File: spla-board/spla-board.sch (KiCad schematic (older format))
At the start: 0 parts

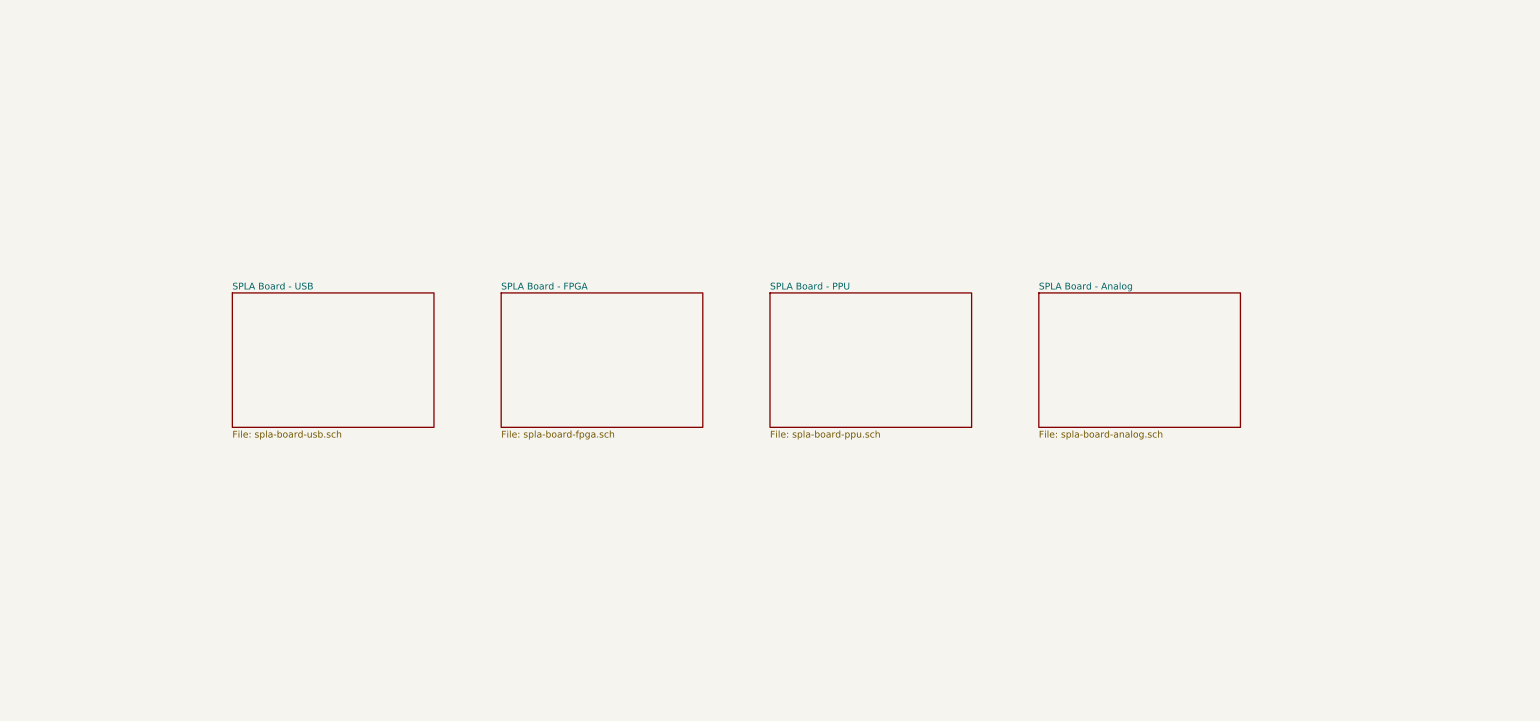
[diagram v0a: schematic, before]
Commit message: schematic: Add blank sheets for future components; rearrange root sheet.
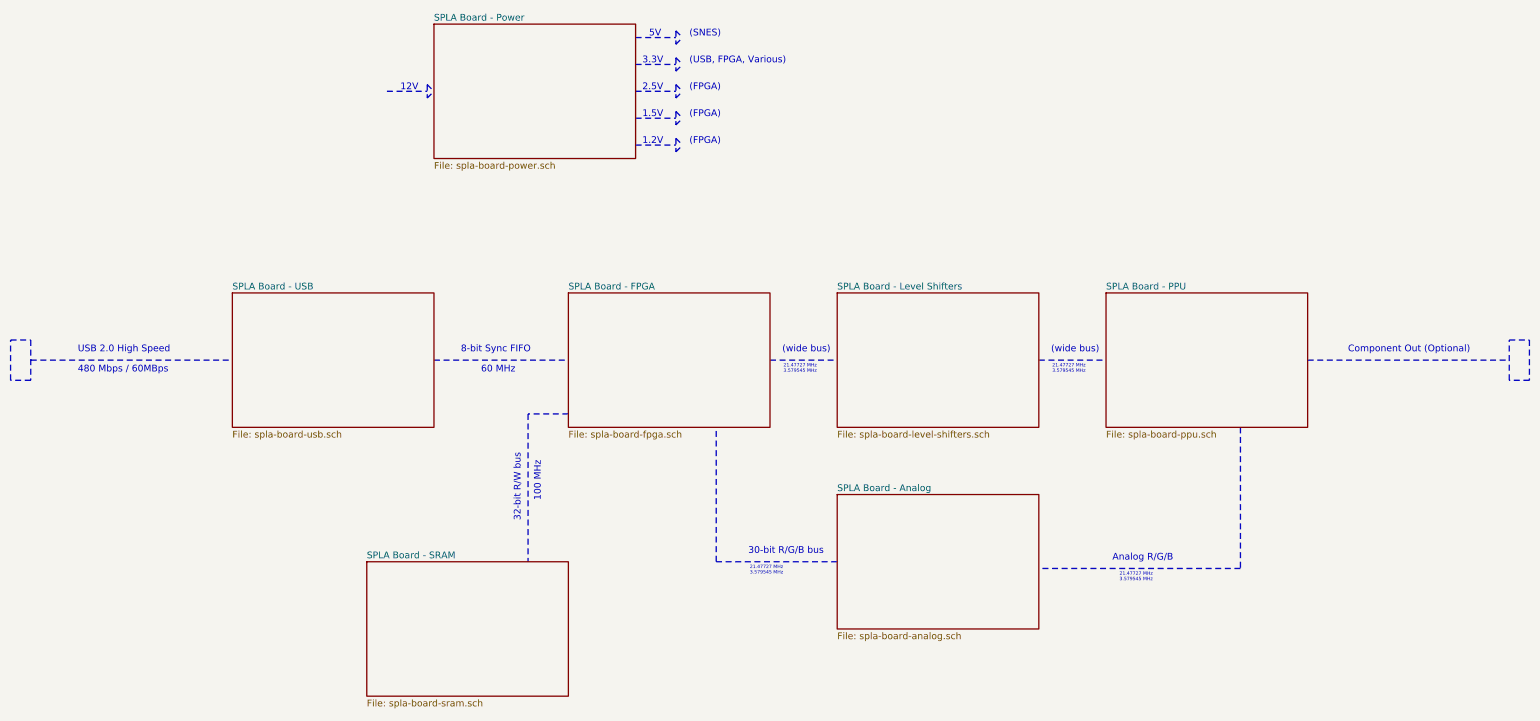
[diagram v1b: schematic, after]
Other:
- note added: "(FPGA)"
- note added: "(SNES)"
- note added: "(USB, FPGA, Various)"
- note added: "(wide bus)"
- note added: "1.2V"
- note added: "1.5V"
- note added: "100 MHz"
- note added: "12V"
- note added: "2.5V"
- note added: "21.47727 MHz\n3.579545 MHz"
- note added: "3.3V"
- note added: "30-bit R/G/B bus"
- note added: "32-bit R/W bus"
- note added: "480 Mbps / 60MBps"
- note added: "5V"
- note added: "60 MHz"
- note added: "8-bit Sync FIFO"
- note added: "Analog R/G/B"
- note added: "Component Out (Optional)"
- note added: "USB 2.0 High Speed"
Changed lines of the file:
@@
 $Descr A3 16535 11693
 encoding utf-8
-Sheet 1 5
+Sheet 1 8
 Title "SPLA Board - Root"
-Date "2020-02-18"
-Rev "2"
+Date "2020-02-21"
+Rev "3"
 Comp ""
 Comment1 ""
@@
 $EndSheet
 $Sheet
-S 6000 4500 1500 1000
+S 6500 4500 1500 1000
 U 5E4D8358
 F0 "SPLA Board - FPGA" 50
@@
 $EndSheet
 $Sheet
-S 8000 4500 1500 1000
+S 10500 4500 1500 1000
 U 5E50E589
 F0 "SPLA Board - PPU" 50
@@
 $EndSheet
 $Sheet
-S 10000 4500 1500 1000
+S 8500 6000 1500 1000
 U 5E520B87
 F0 "SPLA Board - Analog" 50
 F1 "spla-board-analog.sch" 50
 $EndSheet
+$Sheet
+S 5500 2500 1500 1000
+U 5E50D39B
+F0 "SPLA Board - Power" 50
+F1 "spla-board-power.sch" 50
+$EndSheet
+$Sheet
+S 5000 6500 1500 1000
+U 5E50D3C6
+F0 "SPLA Board - SRAM" 50
+F1 "spla-board-sram.sch" 50
+$EndSheet
+Wire Notes Line width 12 style solid
+	2500 5000 4000 5000
+Text Notes 2850 4950 0    50   ~ 0
+USB 2.0 High Speed
+Wire Notes Line width 12 style solid
+	5500 5000 6500 5000
+Wire Notes Line width 12 style solid
+	8000 5000 8500 5000
+$Sheet
+S 8500 4500 1500 1000
+U 5E50D400
+F0 "SPLA Board - Level Shifters" 50
+F1 "spla-board-level-shifters.sch" 50
+$EndSheet
+Wire Notes Line width 12 style solid
+	10000 5000 10500 5000
+Wire Notes Line width 12 style solid
+	11500 5500 11500 6550
+Wire Notes Line width 12 style solid
+	11500 6550 10000 6550
+Wire Notes Line width 12 style solid
+	8500 6500 7600 6500
+Wire Notes Line width 12 style solid
+	7600 6500 7600 5500
+Wire Notes Line width 12 style solid
+	6500 5400 6200 5400
+Wire Notes Line width 12 style solid
+	6200 5400 6200 6500
+Wire Notes Line width 12 style solid
+	12000 5000 13500 5000
+Text Notes 12300 4950 0    50   ~ 0
+Component Out (Optional)
+Text Notes 6150 6200 1    50   ~ 0
+32-bit R/W bus
+Text Notes 5850 5100 0    50   ~ 0
+60 MHz
+Text Notes 8450 4950 2    50   ~ 0
+(wide bus)
+Text Notes 10450 4950 2    50   ~ 0
+(wide bus)
+Text Notes 11000 6500 2    50   ~ 0
+Analog R/G/B
+Text Notes 8400 6450 2    50   ~ 0
+30-bit R/G/B bus
+Wire Notes Line style solid
+	7000 2600 7300 2600
+Wire Notes Line style solid
+	7300 2550 7300 2650
+Wire Notes Line style solid
+	7300 2650 7350 2600
+Wire Notes Line style solid
+	7300 2550 7350 2600
+Wire Notes Line style solid
+	7000 2800 7300 2800
+Wire Notes Line style solid
+	7300 2750 7300 2850
+Wire Notes Line style solid
+	7300 2850 7350 2800
+Wire Notes Line style solid
+	7300 2750 7350 2800
+Wire Notes Line style solid
+	7000 3000 7300 3000
+Wire Notes Line style solid
+	7300 2950 7300 3050
+Wire Notes Line style solid
+	7300 3050 7350 3000
+Wire Notes Line style solid
+	7300 2950 7350 3000
+Wire Notes Line style solid
+	7000 3200 7300 3200
+Wire Notes Line style solid
+	7300 3150 7300 3250
+Wire Notes Line style solid
+	7300 3250 7350 3200
+Wire Notes Line style solid
+	7300 3150 7350 3200
+Text Notes 7100 2600 0    50   ~ 0
+5V
+Text Notes 7050 2800 0    50   ~ 0
+3.3V
+Text Notes 7050 3000 0    50   ~ 0
+2.5V
+Text Notes 7050 3200 0    50   ~ 0
+1.5V
+Wire Notes Line style solid
+	7000 3400 7300 3400
+Wire Notes Line style solid
+	7300 3350 7300 3450
+Wire Notes Line style solid
+	7300 3450 7350 3400
+Wire Notes Line style solid
+	7300 3350 7350 3400
+Text Notes 7050 3400 0    50   ~ 0
+1.2V
+Wire Notes Line style solid
+	5150 3000 5450 3000
+Wire Notes Line style solid
+	5450 2950 5450 3050
+Wire Notes Line style solid
+	5450 3050 5500 3000
+Wire Notes Line style solid
+	5450 2950 5500 3000
+Text Notes 5250 3000 0    50   ~ 0
+12V
+Text Notes 7400 2600 0    50   ~ 0
+(SNES)
+Text Notes 7400 2800 0    50   ~ 0
+(USB, FPGA, Various)
+Text Notes 7400 3000 0    50   ~ 0
+(FPGA)
+Text Notes 7400 3200 0    50   ~ 0
+(FPGA)
+Text Notes 7400 3400 0    50   ~ 0
+(FPGA)
+Text Notes 5700 4950 0    50   ~ 0
+8-bit Sync FIFO
+Text Notes 8100 5100 0    25   ~ 0
+21.47727 MHz\n3.579545 MHz
+Text Notes 10100 5100 0    25   ~ 0
+21.47727 MHz\n3.579545 MHz
+Text Notes 10600 6650 0    25   ~ 0
+21.47727 MHz\n3.579545 MHz
+Text Notes 7850 6600 0    25   ~ 0
+21.47727 MHz\n3.579545 MHz
+Text Notes 6300 6050 1    50   ~ 0
+100 MHz
+Text Notes 2850 5100 0    50   ~ 0
+480 Mbps / 60MBps
+Wire Notes Line width 12 style solid
+	2350 4850 2500 4850
+Wire Notes Line width 12 style solid
+	2500 4850 2500 5150
+Wire Notes Line width 12 style solid
+	2500 5150 2350 5150
+Wire Notes Line width 12 style solid
+	2350 5150 2350 4850
+Wire Notes Line width 12 style solid
+	13500 4850 13650 4850
+Wire Notes Line width 12 style solid
+	13650 4850 13650 5150
+Wire Notes Line width 12 style solid
+	13650 5150 13500 5150
+Wire Notes Line width 12 style solid
+	13500 5150 13500 4850
 $EndSCHEMATC

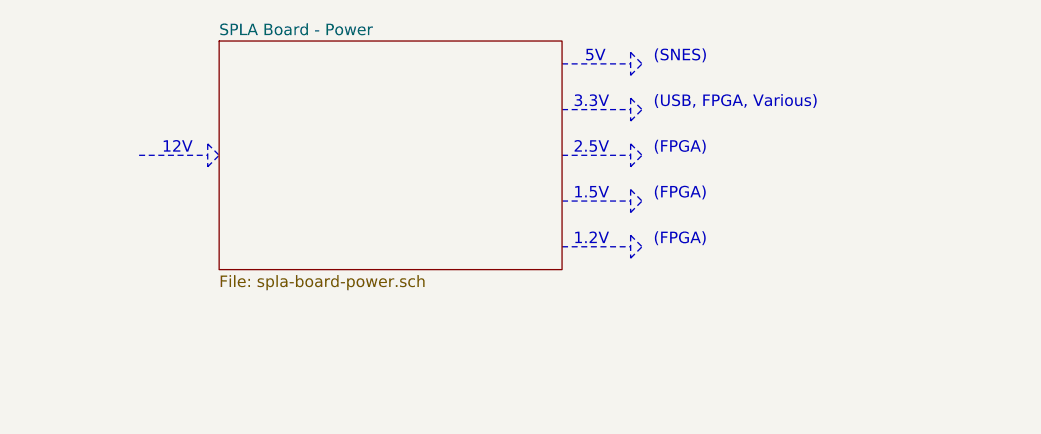
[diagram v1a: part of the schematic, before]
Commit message: schematic: Add power based on a 5V source with TLV733P and MIC2025.
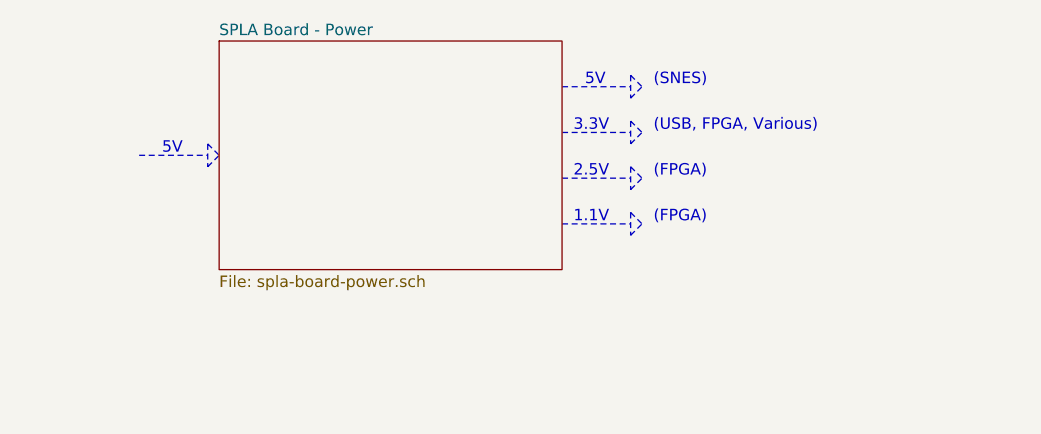
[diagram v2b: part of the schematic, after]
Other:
- note added: "1.1V"
- note removed: "1.2V"
- note removed: "1.5V"
- note removed: "12V"
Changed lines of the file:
@@
 30-bit R/G/B bus
 Wire Notes Line style solid
-	7000 2600 7300 2600
+	7000 2700 7300 2700
 Wire Notes Line style solid
-	7300 2550 7300 2650
+	7300 2650 7300 2750
 Wire Notes Line style solid
-	7300 2650 7350 2600
+	7300 2750 7350 2700
 Wire Notes Line style solid
-	7300 2550 7350 2600
+	7300 2650 7350 2700
 Wire Notes Line style solid
-	7000 2800 7300 2800
+	7000 2900 7300 2900
 Wire Notes Line style solid
-	7300 2750 7300 2850
+	7300 2850 7300 2950
 Wire Notes Line style solid
-	7300 2850 7350 2800
+	7300 2950 7350 2900
 Wire Notes Line style solid
-	7300 2750 7350 2800
+	7300 2850 7350 2900
 Wire Notes Line style solid
-	7000 3000 7300 3000
+	7000 3100 7300 3100
 Wire Notes Line style solid
-	7300 2950 7300 3050
+	7300 3050 7300 3150
 Wire Notes Line style solid
-	7300 3050 7350 3000
+	7300 3150 7350 3100
 Wire Notes Line style solid
-	7300 2950 7350 3000
+	7300 3050 7350 3100
+Text Notes 7100 2700 0    50   ~ 0
+5V
+Text Notes 7050 2900 0    50   ~ 0
+3.3V
+Text Notes 7050 3100 0    50   ~ 0
+2.5V
 Wire Notes Line style solid
-	7000 3200 7300 3200
+	7000 3300 7300 3300
 Wire Notes Line style solid
-	7300 3150 7300 3250
+	7300 3250 7300 3350
 Wire Notes Line style solid
-	7300 3250 7350 3200
+	7300 3350 7350 3300
 Wire Notes Line style solid
-	7300 3150 7350 3200
-Text Notes 7100 2600 0    50   ~ 0
-5V
-Text Notes 7050 2800 0    50   ~ 0
-3.3V
-Text Notes 7050 3000 0    50   ~ 0
-2.5V
-Text Notes 7050 3200 0    50   ~ 0
-1.5V
-Wire Notes Line style solid
-	7000 3400 7300 3400
-Wire Notes Line style solid
-	7300 3350 7300 3450
-Wire Notes Line style solid
-	7300 3450 7350 3400
-Wire Notes Line style solid
-	7300 3350 7350 3400
-Text Notes 7050 3400 0    50   ~ 0
-1.2V
+	7300 3250 7350 3300
+Text Notes 7050 3300 0    50   ~ 0
+1.1V
 Wire Notes Line style solid
 	5150 3000 5450 3000
@@
 	5450 2950 5500 3000
 Text Notes 5250 3000 0    50   ~ 0
-12V
-Text Notes 7400 2600 0    50   ~ 0
+5V
+Text Notes 7400 2700 0    50   ~ 0
 (SNES)
-Text Notes 7400 2800 0    50   ~ 0
+Text Notes 7400 2900 0    50   ~ 0
 (USB, FPGA, Various)
-Text Notes 7400 3000 0    50   ~ 0
+Text Notes 7400 3100 0    50   ~ 0
 (FPGA)
-Text Notes 7400 3200 0    50   ~ 0
-(FPGA)
-Text Notes 7400 3400 0    50   ~ 0
+Text Notes 7400 3300 0    50   ~ 0
 (FPGA)
 Text Notes 5700 4950 0    50   ~ 0

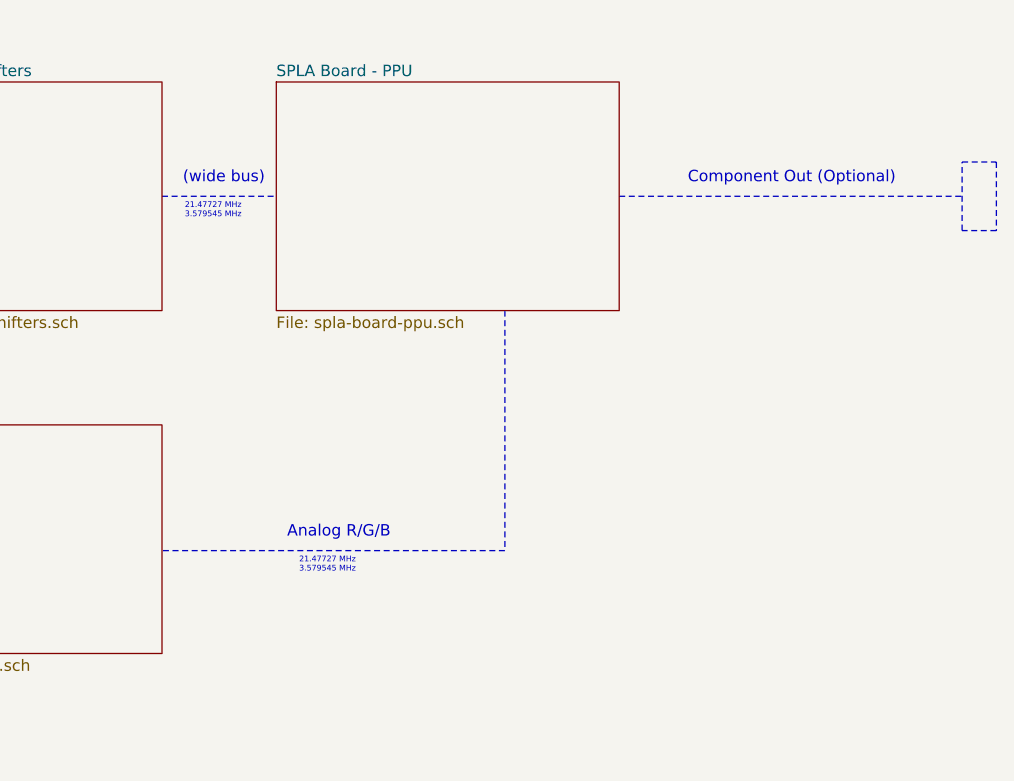
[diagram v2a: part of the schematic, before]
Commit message: schematic: Move around a bunch of IC labels.
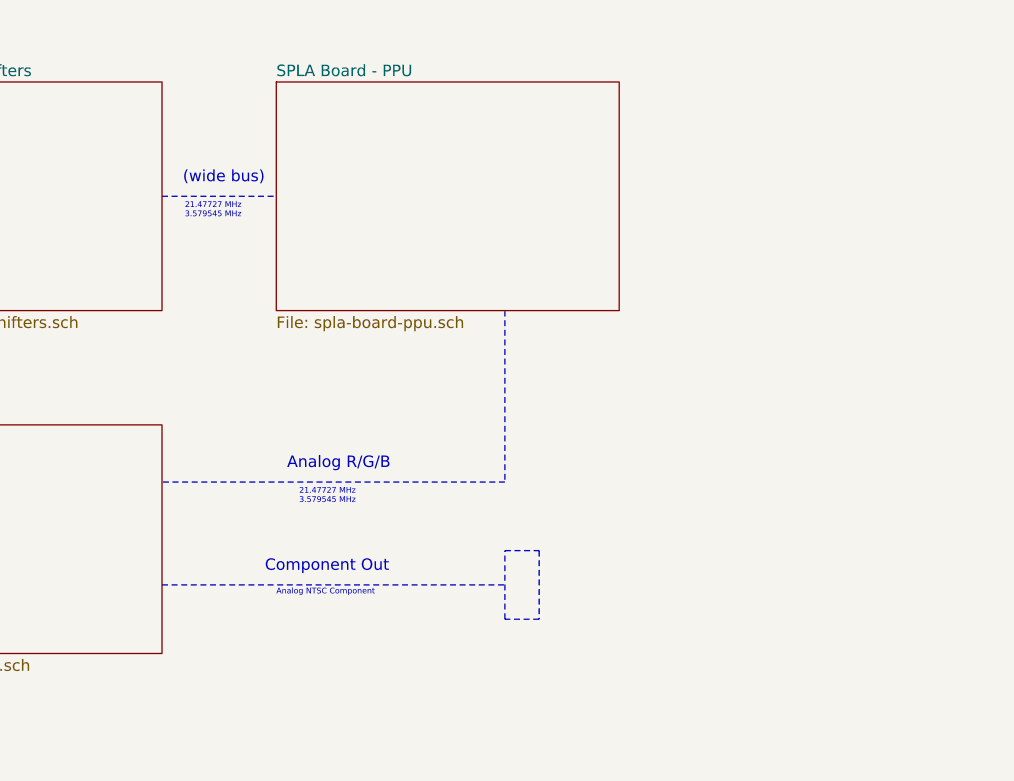
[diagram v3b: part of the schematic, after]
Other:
- note added: "Analog NTSC Component"
- note added: "Component Out"
- note removed: "Component Out (Optional)"
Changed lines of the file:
@@
 	10000 5000 10500 5000
 Wire Notes Line width 12 style solid
-	11500 5500 11500 6550
+	11500 5500 11500 6250
 Wire Notes Line width 12 style solid
-	11500 6550 10000 6550
+	11500 6250 10000 6250
 Wire Notes Line width 12 style solid
 	8500 6500 7600 6500
@@
 	6200 5400 6200 6500
 Wire Notes Line width 12 style solid
-	12000 5000 13500 5000
-Text Notes 12300 4950 0    50   ~ 0
-Component Out (Optional)
+	10000 6700 11500 6700
+Text Notes 10450 6650 0    50   ~ 0
+Component Out
 Text Notes 6150 6200 1    50   ~ 0
 32-bit R/W bus
@@
 Text Notes 10450 4950 2    50   ~ 0
 (wide bus)
-Text Notes 11000 6500 2    50   ~ 0
+Text Notes 11000 6200 2    50   ~ 0
 Analog R/G/B
 Text Notes 8400 6450 2    50   ~ 0
@@
 Text Notes 10100 5100 0    25   ~ 0
 21.47727 MHz\n3.579545 MHz
-Text Notes 10600 6650 0    25   ~ 0
+Text Notes 10600 6350 0    25   ~ 0
 21.47727 MHz\n3.579545 MHz
 Text Notes 7850 6600 0    25   ~ 0
@@
 	2350 5150 2350 4850
 Wire Notes Line width 12 style solid
-	13500 4850 13650 4850
+	11500 6550 11650 6550
 Wire Notes Line width 12 style solid
-	13650 4850 13650 5150
+	11650 6550 11650 6850
 Wire Notes Line width 12 style solid
-	13650 5150 13500 5150
+	11650 6850 11500 6850
 Wire Notes Line width 12 style solid
-	13500 5150 13500 4850
+	11500 6850 11500 6550
+Text Notes 10500 6750 0    25   ~ 0
+Analog NTSC Component
 $EndSCHEMATC
